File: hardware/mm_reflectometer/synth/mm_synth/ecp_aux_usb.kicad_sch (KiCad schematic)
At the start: 40 parts, among them J2101 USB_C_Receptacle_USB2.0, Q2101 VBZA4435, U1601 ECP5U_25_CABGA256, U2101 HUSB238, X2101 ASE-xxxMHz

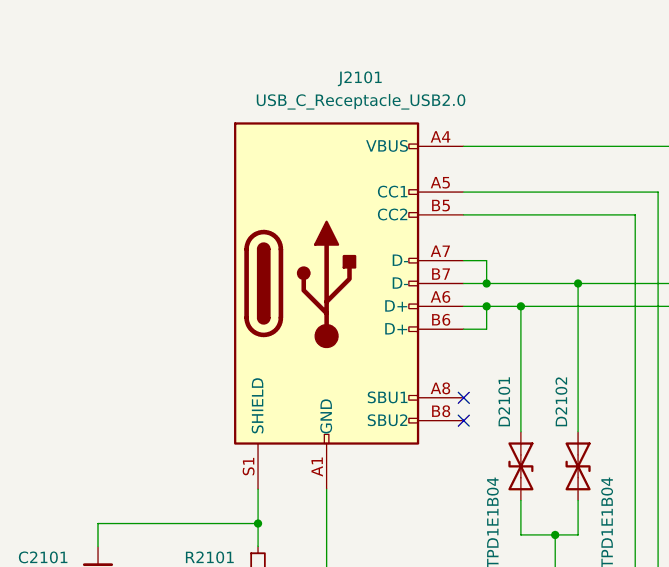
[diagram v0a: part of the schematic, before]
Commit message: more component placement on mm synth
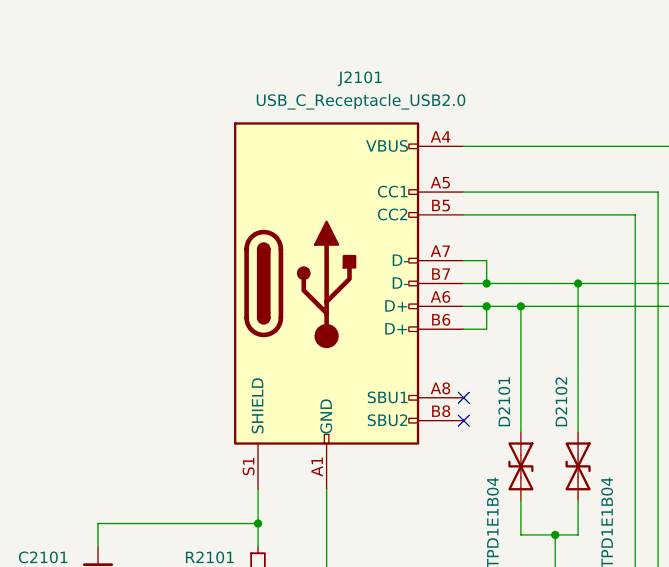
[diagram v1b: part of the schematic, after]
